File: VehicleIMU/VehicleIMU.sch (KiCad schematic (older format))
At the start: 35 parts, among them J1 RJ45, J2 RJ45, P1 CONN_01X04, P2 CONN_01X02, P3 CONN_02X03, Q1 Q_PMOS_DSG, SW1 SW_PUSH, U1 FGMMOPA6H, U2 MS5611, U3 MPU-9250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

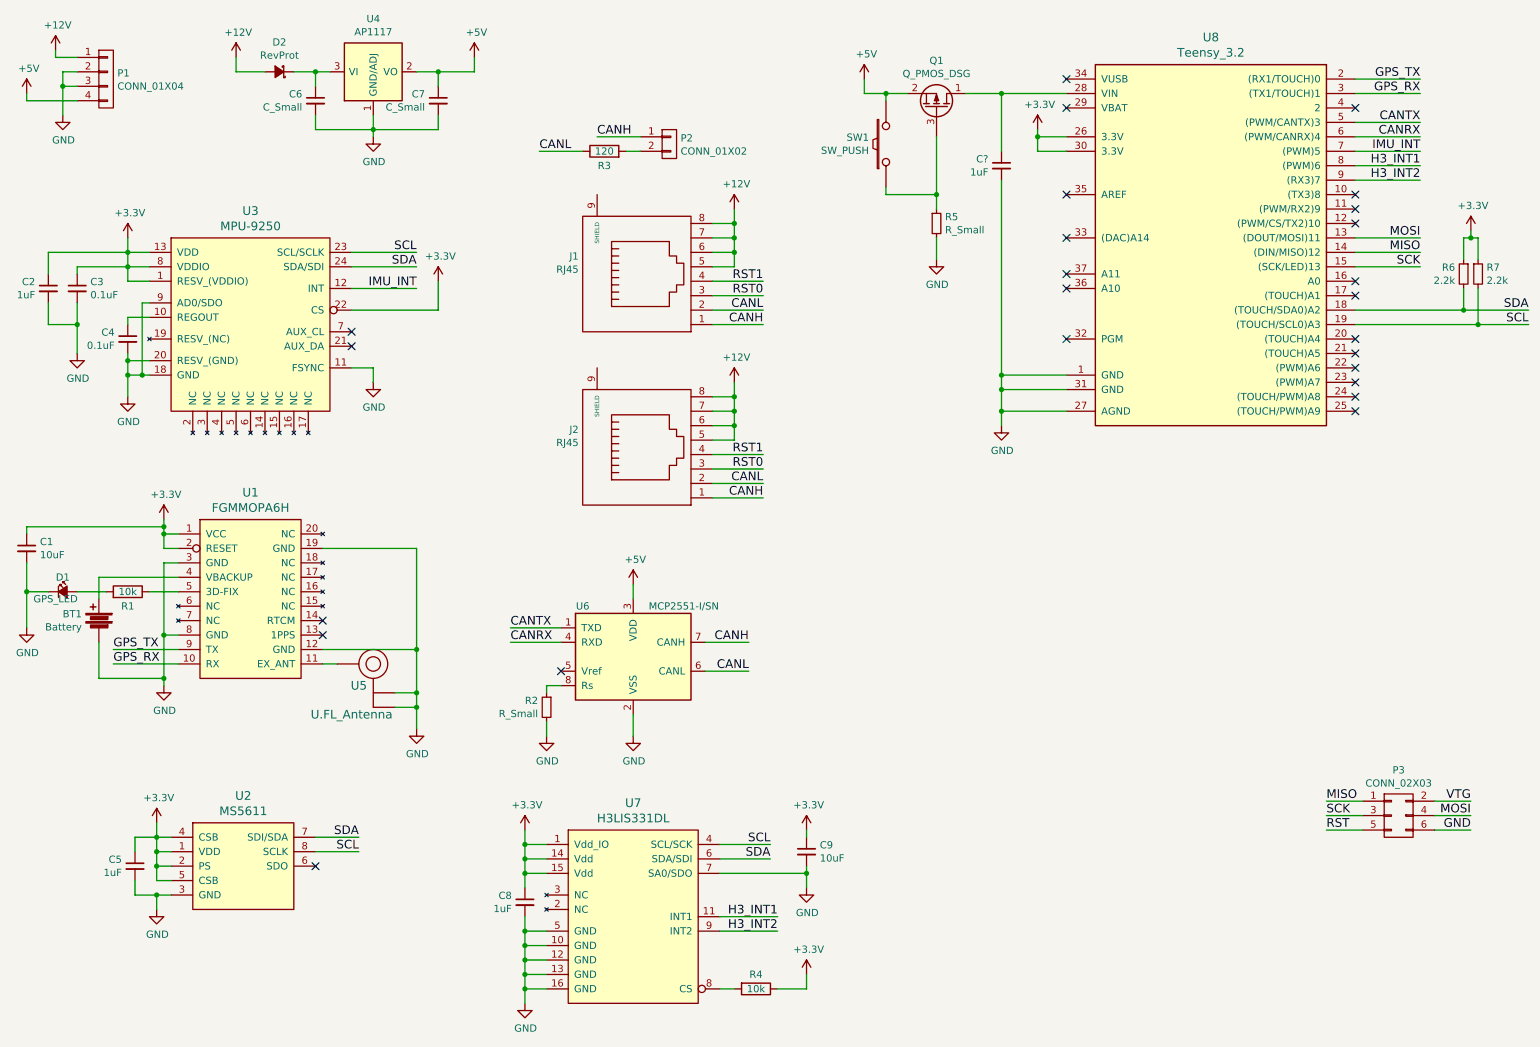
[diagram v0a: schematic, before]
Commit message: Changes to VehicleIMU, create CAT6_Adapter
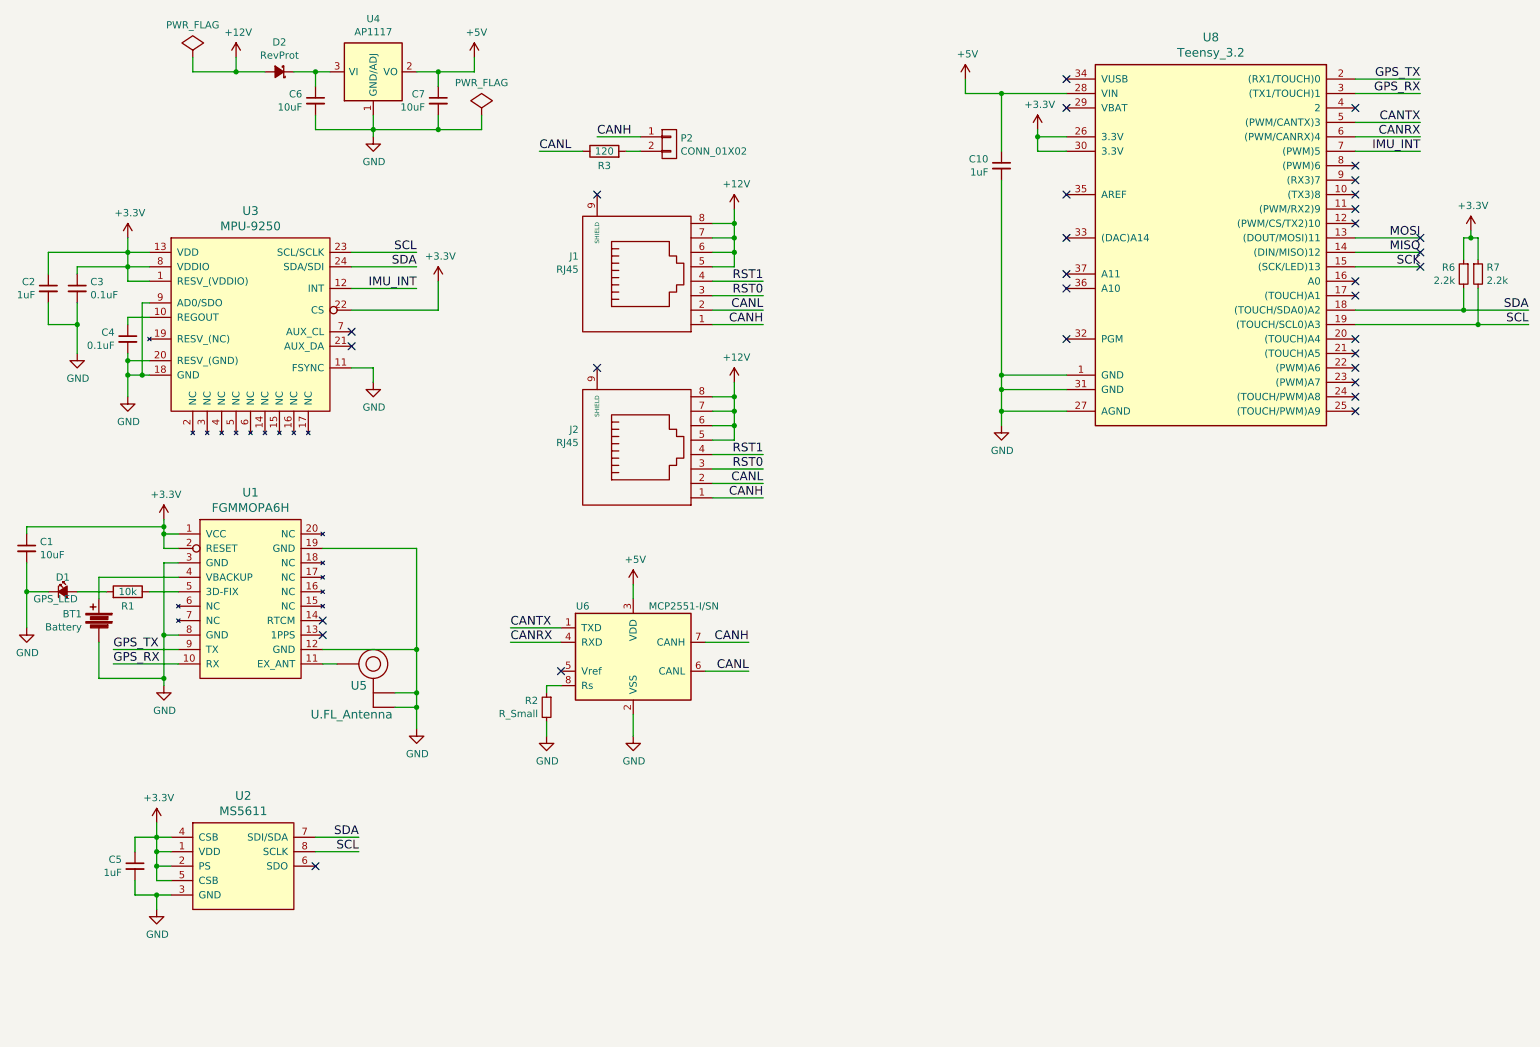
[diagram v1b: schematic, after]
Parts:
- removed C8: 1uF, symbol C_Small
- removed C9: 10uF, symbol C_Small
- removed P1: CONN_01X04, symbol CONN_01X04
- removed P3: CONN_02X03, symbol CONN_02X03
- removed Q1: Q_PMOS_DSG, symbol Q_PMOS_DSG
- removed R4: 10k, symbol R
- removed R5: R_Small, symbol R_Small
- removed SW1: SW_PUSH, symbol SW_PUSH
- removed U7: H3LIS331DL, symbol H3LIS331DL
- BT1: footprint (none) -> Connect:CR1220
- C1, C2, C3, C4, C5: footprint (none) -> Capacitors_SMD:C_0805
- C10: renamed from C?; footprint (none) -> Capacitors_SMD:C_0805
- C6, C7: value C_Small -> 10uF; footprint (none) -> Capacitors_SMD:C_0805
- D1: footprint (none) -> LEDs:LED_0805
- D2: footprint (none) -> Diodes_SMD:SOD-123
- J1, J2: footprint (none) -> UNCAMotorsports:8P8C_SHD
- P2: footprint (none) -> Pin_Headers:Pin_Header_Straight_1x02
- R1, R2, R3, R6, R7: footprint (none) -> Resistors_SMD:R_0805
- U1: footprint (none) -> Wetmelon:FGPMMOPA6H
- U2: footprint (none) -> UNCAMotorsports:MS5611
- U3: footprint (none) -> UNCAMotorsports:MPU-9250
- U5: footprint (none) -> UNCAMotorsports:U.FL-CON
- U8: footprint (none) -> UNCAMotorsports:Teensy_3.2+4
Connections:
- net +5V: now also C10.1, U8.28 (VIN)
- net H3_INT1: no longer names the net of U8.8 ((PWM)6)
- net H3_INT2: no longer names the net of U8.9 ((RX3)7)
- no-connect marks 25 -> 32
